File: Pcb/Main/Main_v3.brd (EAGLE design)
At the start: 63.5 x 76.1 mm, 60 parts, among them IC1 CC3220MODASF12MONR, J1 CORTEX_JTAG_DEBUG_PTH, J5 MOLEX_43045-0200MOLEX_43045-0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, Q1 220mA/50V/3.5Ω, U1 AD7993BRU-0, U2 LTC3440EMSPBF, U3 MAX17201G+T

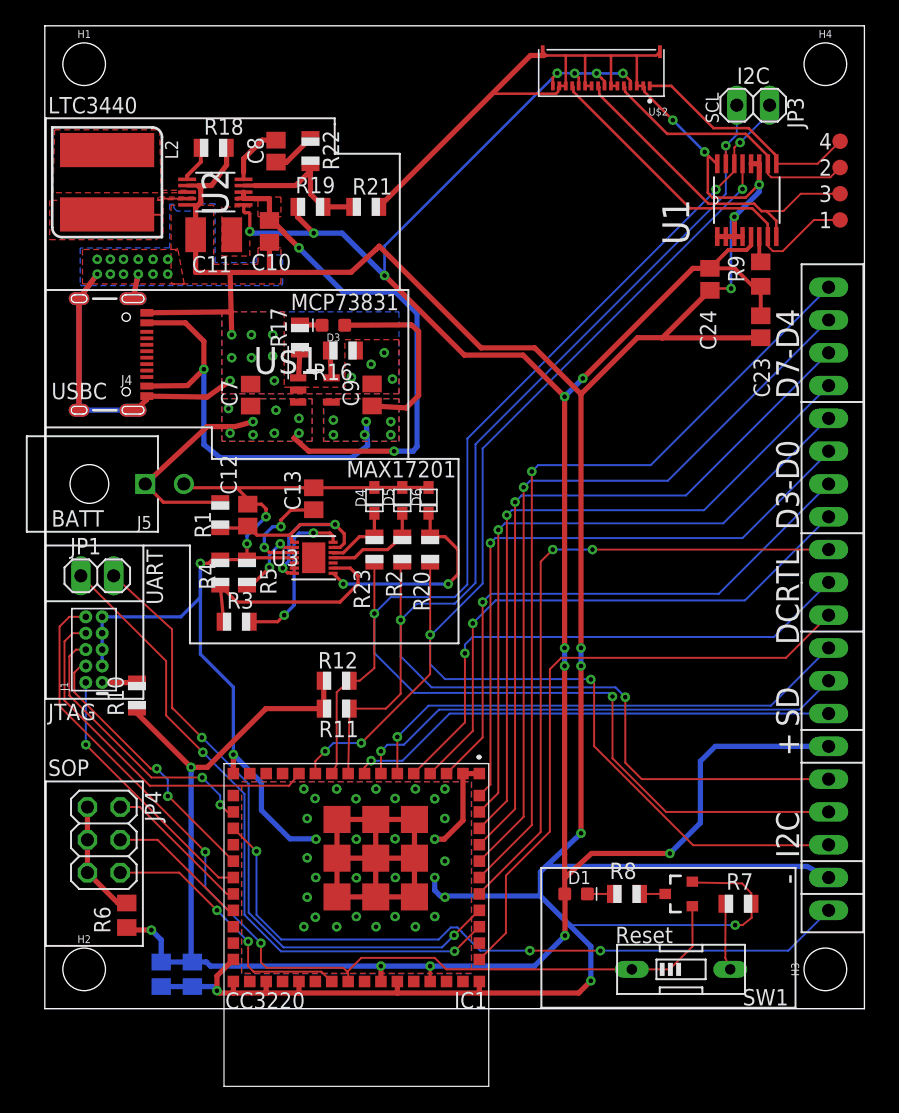
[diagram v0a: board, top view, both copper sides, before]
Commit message: Updated PCB files and ported some of the graphics functions. The graphics changes are not tested yet.
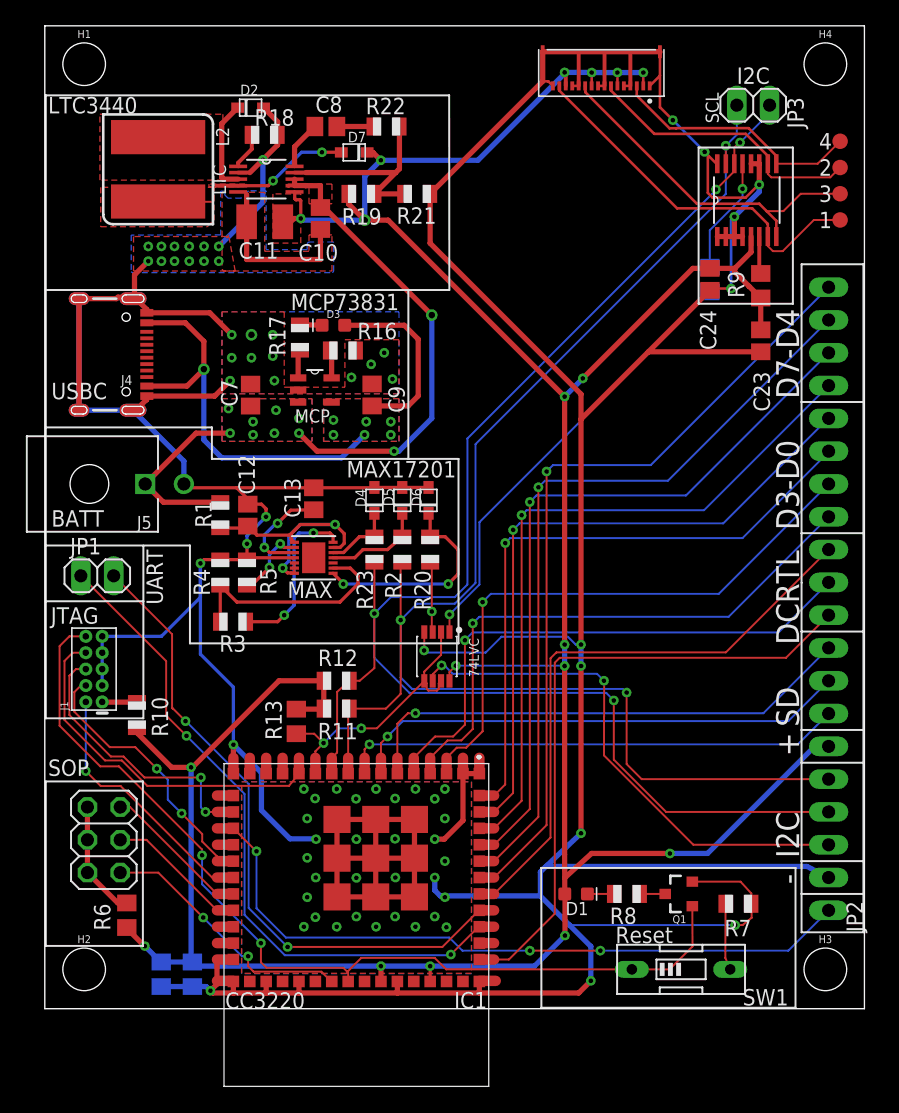
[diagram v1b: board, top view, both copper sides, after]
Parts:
- removed U2: LTC3440EMSPBF, LTC3440EMSPBF:SOP50P490X110-10N
- added 74LVC: SOP65P400X110-8N, SOP65P400X110-8N:SOP65P400X110-8N
- added D2, D7: (no value), adafruit:SOD-323F
- added LTC: LTC3440EMSPBF, LTC3440EMSPBF:SOP50P490X110-10N
- added R13: 10k, rcl:R0805
- added R14: 1k, rcl:R0805
- R6: value (none) -> 10k
- moved R22 6.19 mm to (26.5, 68.3), turned to 180 degrees
- moved C8 4.31 mm to (21.8, 68.3), turned to 0 degrees
- moved L2 4.08 mm to (8.78, 65.0)
- moved C10 4.08 mm to (21.3, 61.2)
- moved C11 4.08 mm to (17.0, 60.9)
- moved R18 4.08 mm to (17.0, 67.7)
- moved R19 4.08 mm to (24.5, 63.1)
- moved R21 4.08 mm to (28.8, 63.1)
- moved R10 1.51 mm to (7.14, 22.7)
- moved J1 1.51 mm to (3.81, 26.3)
- moved C23 1.09 mm to (55.4, 51.7)
- moved R9 0.90 mm to (55.4, 56.0)
- moved R3 0.28 mm to (14.6, 30.0)
- turned H3 to 0 degrees
- renumbered U$1 to MCP, U3 to MAX
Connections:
- new net I2C_ADC: 74LVC.1, R14.1
- new net I2C_DSP: 74LVC.6, JP2.3
- new net I2C_MAX: 74LVC.3, R20.2
- new net N$10: IC1.25
- new net N$11: IC1.26
- new net N$12: IC1.29
- new net N$13: IC1.31
- new net N$14: IC1.17
- new net N$15: IC1.15
- new net N$16: IC1.14
- new net N$17: IC1.13
- new net N$18: IC1.20
- new net N$3: IC1.41
- new net N$4: R14.2, U1.13
- new net N$5: IC1.42
- new net N$6: IC1.39
- new net N$7: IC1.36
- new net N$8: IC1.33
- new net N$9: IC1.45
- net GND: now also 74LVC.4, D2.A, LTC.2, LTC.5, U$2.1, U$2.12, U$2.13, U$2.16, U$2.4, U$2.5, U$2.8, U$2.9; no longer U$2.10, U$2.11, U$2.14, U$2.15, U$2.2, U$2.3, U$2.6, U$2.7, U2.2, U2.5
- net I2C_INT: now also 74LVC.2, 74LVC.5, 74LVC.7, R13.2; no longer JP2.3, R20.2, U1.13
- net LTC_FB: now also LTC.9; no longer U2.9
- net LTC_IND1: now also D2.C, LTC.3; no longer U2.3
- net LTC_IND2: now also D7.A, LTC.4; no longer U2.4
- net LTC_RT: now also LTC.1; no longer U2.1
- net LTC_VC: now also LTC.10; no longer U2.10
- net VBAT: now also LTC.7, LTC.8; no longer U2.7, U2.8
- net VCC: now also 74LVC.8, D7.C, LTC.6, R13.1, U$2.10, U$2.14, U$2.2, U$2.6; no longer U$2.12, U$2.16, U$2.4, U$2.8, U2.6
- net VIN1: now also U$2.15; no longer U$2.13
- net VIN2: now also U$2.7; no longer U$2.5
- net VIN3: now also U$2.11; no longer U$2.9
- net VIN4: now also U$2.3; no longer U$2.1
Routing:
- net I2C_INT: track 109.7 -> 21.6 mm, vias 5 -> 2
- net I2C_DSP: track 0.00 -> 40.6 mm, vias 0 -> 2
- net I2C_ADC: track 0.00 -> 34.7 mm, vias 0 -> 1
- net GND: track 466.7 -> 483.3 mm, vias 70 -> 73
- net N$4: track 0.00 -> 9.07 mm, vias 0 -> 1
- net LTC_IND2: track 7.52 -> 16.4 mm, vias 0 -> 2
- net VCC: track 236.9 -> 245.5 mm, vias 17 -> 18
- net LTC_IND1: track 0.00 -> 7.25 mm
- net I2C_MAX: track 0.00 -> 5.51 mm, vias 0 -> 1
- net VBAT: track 56.1 -> 51.0 mm
- net DCX: track 50.4 -> 46.3 mm, vias 2 -> 0
- net LTC_FB: track 12.2 -> 16.2 mm
- net VBUS: track 48.1 -> 45.8 mm
- net VIN4: track 18.3 -> 19.8 mm
- net WRX: track 48.1 -> 49.5 mm
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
